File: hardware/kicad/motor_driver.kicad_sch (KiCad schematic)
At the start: 17 parts, among them J1 Conn_01x05_Pin, J2 TO_MOTOR, J3 5V_IN, J4 PRT-10811, U1 ULN2003A

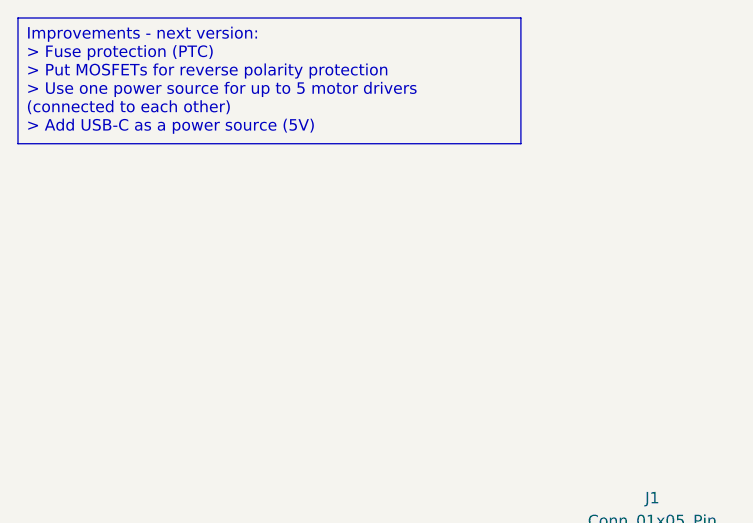
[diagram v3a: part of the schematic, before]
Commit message: feat: added pcb board and components placements
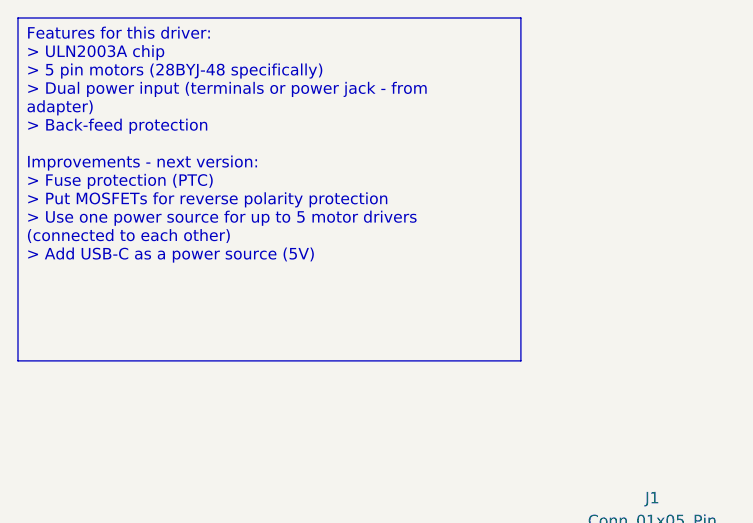
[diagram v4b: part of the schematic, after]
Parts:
- C1: footprint (none) -> Capacitor_THT:C_Rect_L4.6mm_W3.0mm_P2.50mm_MKS02_FKP02
- C2: footprint (none) -> Capacitor_THT:CP_Radial_D8.0mm_P3.50mm
- D1, D2: footprint (none) -> Diode_THT:D_DO-201AD_P15.24mm_Horizontal
- J4: footprint PRT-10811_SPK -> Power Jack:PRT-10811_SPK
- R1, R2, R3, R4, R5, R6, R7, R8: footprint (none) -> Resistor_THT:R_Axial_DIN0207_L6.3mm_D2.5mm_P10.16mm_Horizontal
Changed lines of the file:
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@@
 	(generator_version "9.0")
 	(paper "A4")
-	(text_box "Improvements - next version:\n> Fuse protection (PTC)\n> Put MOSFETs for reverse polarity protection\n> Use one power source for up to 5 motor drivers (connected to each other)\n> Add USB-C as a power source (5V)"
+	(text_box "Features for this driver:\n> ULN2003A chip\n> 5 pin motors (28BYJ-48 specifically)\n> Dual power input (terminals or power jack - from adapter)\n> Back-feed protection\n\nImprovements - next version:\n> Fuse protection (PTC)\n> Put MOSFETs for reverse polarity protection\n> Use one power source for up to 5 motor drivers (connected to each other)\n> Add USB-C as a power source (5V)"
 		(exclude_from_sim no)
 		(at 15.24 13.97 0)
-		(size 55.88 13.97)
+		(size 55.88 38.1)
 		(margins 0.9525 0.9525 0.9525 0.9525)
 		(stroke
@@
 			)
 		)
-		(property "Footprint" ""
+		(property "Footprint" "Capacitor_THT:C_Rect_L4.6mm_W3.0mm_P2.50mm_MKS02_FKP02"
 			(at 146.3548 88.9 0)
 			(effects
@@
 			)
 		)
-		(property "Footprint" ""
+		(property "Footprint" "Diode_THT:D_DO-201AD_P15.24mm_Horizontal"
 			(at 168.91 45.72 0)
 			(effects
@@
 			)
 		)
-		(property "Footprint" ""
+		(property "Footprint" "Capacitor_THT:CP_Radial_D8.0mm_P3.50mm"
 			(at 154.6352 88.9 0)
 			(effects
@@
 			)
 		)
-		(property "Footprint" ""
+		(property "Footprint" "Resistor_THT:R_Axial_DIN0207_L6.3mm_D2.5mm_P10.16mm_Horizontal"
 			(at 100.33 81.788 90)
 			(effects
@@
 			)
 		)
-		(property "Footprint" "PRT-10811_SPK"
+		(property "Footprint" "Power Jack:PRT-10811_SPK"
 			(at 180.34 45.72 0)
 			(effects
@@
 			)
 		)
-		(property "Footprint" ""
+		(property "Footprint" "Resistor_THT:R_Axial_DIN0207_L6.3mm_D2.5mm_P10.16mm_Horizontal"
 			(at 107.188 93.98 90)
 			(effects
@@
 			)
 		)
-		(property "Footprint" ""
+		(property "Footprint" "Resistor_THT:R_Axial_DIN0207_L6.3mm_D2.5mm_P10.16mm_Horizontal"
 			(at 100.33 74.168 90)
 			(effects
@@
 			)
 		)
-		(property "Footprint" ""
+		(property "Footprint" "Resistor_THT:R_Axial_DIN0207_L6.3mm_D2.5mm_P10.16mm_Horizontal"
 			(at 109.728 93.98 90)
 			(effects
@@
 			)
 		)
-		(property "Footprint" ""
+		(property "Footprint" "Resistor_THT:R_Axial_DIN0207_L6.3mm_D2.5mm_P10.16mm_Horizontal"
 			(at 112.268 93.98 90)
 			(effects
@@
 			)
 		)
-		(property "Footprint" ""
+		(property "Footprint" "Resistor_THT:R_Axial_DIN0207_L6.3mm_D2.5mm_P10.16mm_Horizontal"
 			(at 100.33 79.248 90)
 			(effects
@@
 			)
 		)
-		(property "Footprint" ""
+		(property "Footprint" "Diode_THT:D_DO-201AD_P15.24mm_Horizontal"
 			(at 170.18 62.23 0)
 			(effects
@@
 			)
 		)
-		(property "Footprint" ""
+		(property "Footprint" "Resistor_THT:R_Axial_DIN0207_L6.3mm_D2.5mm_P10.16mm_Horizontal"
 			(at 114.808 93.98 90)
 			(effects
@@
 			)
 		)
-		(property "Footprint" ""
+		(property "Footprint" "Resistor_THT:R_Axial_DIN0207_L6.3mm_D2.5mm_P10.16mm_Horizontal"
 			(at 100.33 76.708 90)
 			(effects

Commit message: perf: routed the components - PCB
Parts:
- removed J4: PRT-10811, Power Jack:PRT-10811_SPK, symbol Power Jack:PRT-10811
- added J4: DC-005-5A-2.0, DC-005-5A-2.0:XKB_DC-005-5A-2.0, symbol Power Jack:DC-005-5A-2.0
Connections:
- net +5V_COM: now reaches C1.1, C2.1, D1.1 (K), D2.1 (K), J2.1 (Pin_1), U1.9 (COM)
- net GND: now reaches C1.2, C2.2, J1.5 (Pin_5), J3.2 (Pin_2), R5.1, R6.1, R7.1, R8.1, U1.8 (GND)
- net GND: now also J4.2, J4.3
- net at D1.2 (A): now also J4.1
- net IN4: now reaches J1.4 (Pin_4), R4.1
- net IN1: now reaches J1.1 (Pin_1), R1.1
- net IN3: now reaches J1.3 (Pin_3), R3.1
- net IN2: now reaches J1.2 (Pin_2), R2.1
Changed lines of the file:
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@@
+		)
+	)
+	(label "IN3"
+		(at 93.98 77.47 0)
+		(effects
+			(font
+				(size 1.27 1.27)
+			)
+			(justify left bottom)
+		)
+	)
+	(label "+5V_COM"
+		(at 138.43 67.31 0)
+		(effects
+			(font
+				(size 1.27 1.27)
+			)
+			(justify left bottom)
+		)
+	)
+	(label "IN4"
+		(at 93.98 80.01 0)
+		(effects
+			(font
+				(size 1.27 1.27)
+			)
+			(justify left bottom)
+		)
+	)
+	(label "GND"
+		(at 93.98 82.55 0)
+		(effects
+			(font
+				(size 1.27 1.27)
+			)
+			(justify left bottom)
+		)
+	)
+	(label "IN2"
+		(at 93.98 74.93 0)
+		(effects
+			(font
+				(size 1.27 1.27)
+			)
+			(justify left bottom)
+		)
+	)
+	(label "IN1"
+		(at 93.98 72.39 0)
+		(effects
+			(font
+				(size 1.27 1.27)
+			)
+			(justify left bottom)
 		)
 	)
@@
 	)
 	(symbol
-		(lib_id "Power Jack:PRT-10811")
-		(at 180.34 45.72 180)
-		(unit 1)
-		(exclude_from_sim no)
-		(in_bom yes)
-		(on_board yes)
-		(dnp no)
-		(fields_autoplaced yes)
-		(property "Reference" "J4"
-			(at 212.09 41.9099 0)
-			(effects
-				(font
-					(size 1.524 1.524)
-				)
-				(justify right)
-			)
-		)
-		(property "Value" "PRT-10811"
-			(at 212.09 44.4499 0)
-			(effects
-				(font
-					(size 1.524 1.524)
-				)
-				(justify right)
-			)
-		)
-		(property "Footprint" "Power Jack:PRT-10811_SPK"
-			(at 180.34 45.72 0)
-			(effects
-				(font
-					(size 1.27 1.27)
-					(italic yes)
-				)
-				(hide yes)
-			)
-		)
-		(property "Datasheet" "PRT-10811"
-			(at 180.34 45.72 0)
-			(effects
-				(font
-					(size 1.27 1.27)
-					(italic yes)
-				)
-				(hide yes)
-			)
-		)
-		(property "Description" ""
-			(at 180.34 45.72 0)
-			(effects
-				(font
-					(size 1.27 1.27)
-				)
-				(hide yes)
-			)
-		)
-		(pin "3"
-		)
-		(pin "2"
-		)
-		(pin "1"
-		)
-		(instances
-			(project ""
-				(path "/b7a12314-1361-4fdf-a1f9-9f4ac4cac78f"
-					(reference "J4")
-					(unit 1)
-				)
-			)
-		)
-	)
-	(symbol
 		(lib_id "power:PWR_FLAG")
 		(at 179.07 40.64 0)
@@
 					(unit 1)
 				)
+			)
+		)
+	)
+	(symbol
+		(lib_id "Power Jack:DC-005-5A-2.0")
+		(at 187.96 43.18 180)
+		(unit 1)
+		(exclude_from_sim no)
+		(in_bom yes)
+		(on_board yes)
+		(dnp no)
+		(property "Reference" "J4"
+			(at 188.7311 52.07 0)
+			(effects
+				(font
+					(size 1.27 1.27)
+				)
+			)
+		)
+		(property "Value" "DC-005-5A-2.0"
+			(at 188.7311 49.53 0)
+			(effects
+				(font
+					(size 1.27 1.27)
+				)
+			)
+		)
+		(property "Footprint" "DC-005-5A-2.0:XKB_DC-005-5A-2.0"
+			(at 187.96 43.18 0)
+			(effects
+				(font
+					(size 1.27 1.27)
+				)
+				(justify bottom)
+				(hide yes)
+			)
+		)
+		(property "Datasheet" ""
+			(at 187.96 43.18 0)
+			(effects
+				(font
+					(size 1.27 1.27)
+				)
+				(hide yes)
+			)
+		)
+		(property "Description" ""
+			(at 187.96 43.18 0)
+			(effects
+				(font
+					(size 1.27 1.27)
+				)
+				(hide yes)
+			)
+		)
+		(property "MF" "XKB Industrial Precision"
+			(at 187.96 43.18 0)
+			(effects
+				(font
+					(size 1.27 1.27)
+				)
+				(justify bottom)
+				(hide yes)
+			)
+		)
+		(property "MAXIMUM_PACKAGE_HEIGHT" "11 mm"
+			(at 187.96 43.18 0)
+			(effects
+				(font
+					(size 1.27 1.27)
+				)
+				(justify bottom)
+				(hide yes)
+			)
+		)
+		(property "Package" "Package"
+			(at 187.96 43.18 0)
+			(effects
+				(font
+					(size 1.27 1.27)
+				)
+				(justify bottom)
+				(hide yes)
+			)
+		)
+		(property "Price" "None"
+			(at 187.96 43.18 0)
+			(effects
+				(font
+					(size 1.27 1.27)
+				)
+				(justify bottom)
+				(hide yes)
+			)
+		)
+		(property "Check_prices" "https://www.snapeda.com/parts/DC-005-5A-2.0/XKB+Connection/view-part/?ref=eda"
+			(at 187.96 43.18 0)
+			(effects
+				(font
+					(size 1.27 1.27)
+				)
+				(justify bottom)
+				(hide yes)
+			)
+		)
+		(property "STANDARD" "Manufacturer Recommendations"
+			(at 187.96 43.18 0)
+			(effects
+				(font
+					(size 1.27 1.27)
+				)
+				(justify bottom)
+				(hide yes)
+			)
+		)
+		(property "PARTREV" "A0"
+			(at 187.96 43.18 0)
+			(effects
+				(font
+					(size 1.27 1.27)
+				)
+				(justify bottom)
+				(hide yes)
+			)
+		)
+		(property "SnapEDA_Link" "https://www.snapeda.com/parts/DC-005-5A-2.0/XKB+Connection/view-part/?ref=snap"
+			(at 187.96 43.18 0)
+			(effects
+				(font
+					(size 1.27 1.27)
+				)
+				(justify bottom)
+				(hide yes)
+			)
+		)
+		(property "MP" "DC-005-5A-2.0"
+			(at 187.96 43.18 0)
+			(effects
+				(font
+					(size 1.27 1.27)
+				)
+				(justify bottom)
+				(hide yes)
+			)
+		)
+		(property "Description_1" "DC Power Receptacle Jack, Through Hole，Right Angle"
+			(at 187.96 43.18 0)
+			(effects
+				(font
+					(size 1.27 1.27)
+				)
+				(justify bottom)
+				(hide yes)
+			)
+		)
+		(property "Availability" "Not in stock"
+			(at 187.96 43.18 0)
+			(effects
+				(font
+					(size 1.27 1.27)
+				)
+				(justify bottom)
+				(hide yes)
+			)
+		)
+		(property "MANUFACTURER" "XKB"
+			(at 187.96 43.18 0)
+			(effects
+				(font
+					(size 1.27 1.27)
+				)
+				(justify bottom)
+				(hide yes)
+			)
+		)
+		(pin "1"
+		)
+		(pin "3"
+		)
+		(pin "2"
+		)
+		(instances
+			(project ""
+				(path "/b7a12314-1361-4fdf-a1f9-9f4ac4cac78f"
+					(reference "J4")
+					(unit 1)
+				)

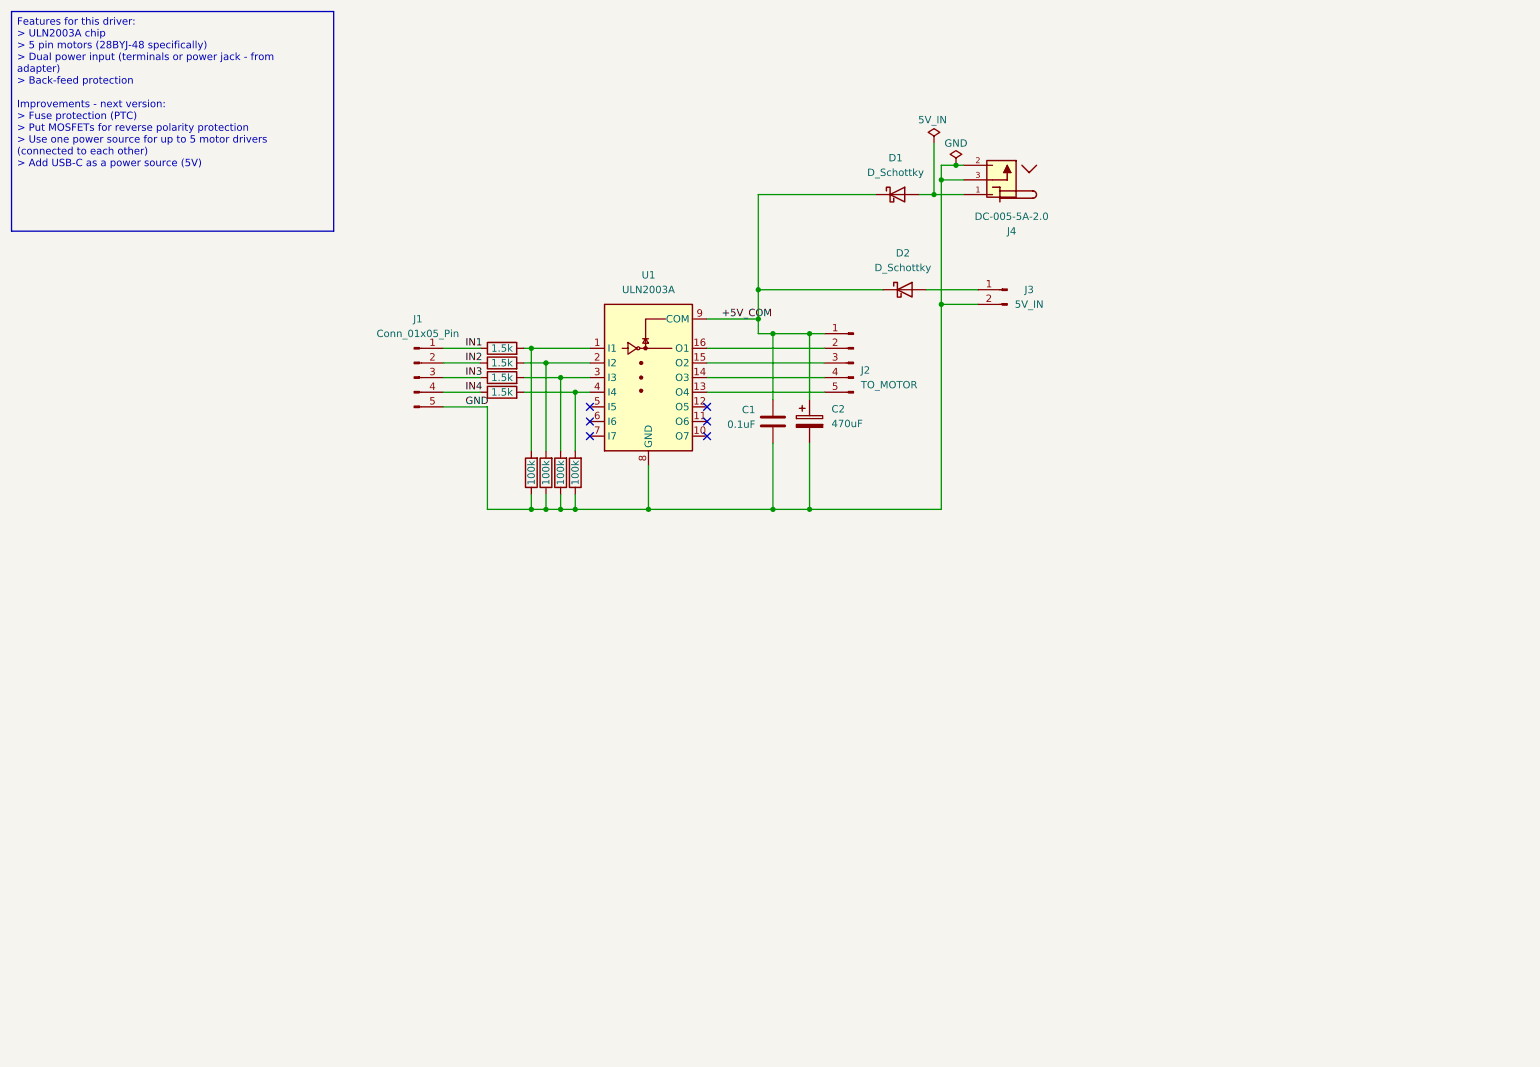
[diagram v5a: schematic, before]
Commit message: docs: added exports schematic & pcb
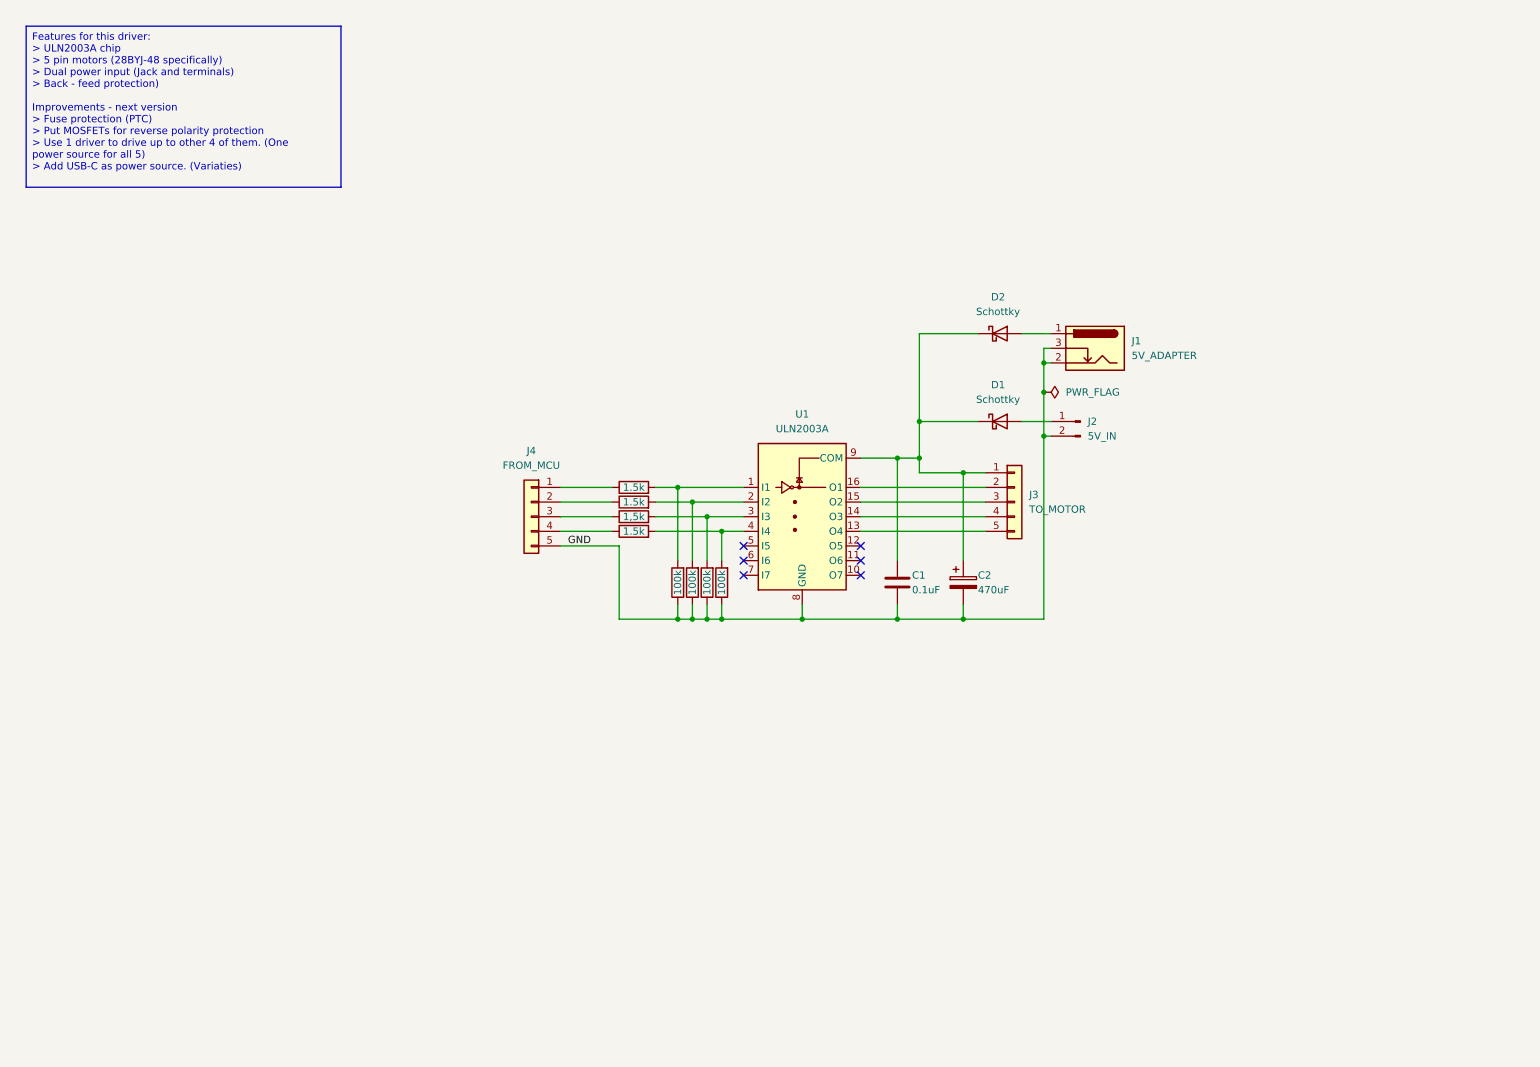
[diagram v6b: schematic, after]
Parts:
- removed J1: Conn_01x05_Pin, Connector_PinHeader_2.54mm:PinHeader_1x05_P2.54mm_Vertical, symbol Connector:Conn_01x05_Pin
- removed J2: TO_MOTOR, Connector_JST:JST_XH_B5B-XH-A_1x05_P2.50mm_Vertical, symbol Connector:Conn_01x05_Pin
- removed J3: 5V_IN, Connector_PinHeader_2.54mm:PinHeader_1x02_P2.54mm_Vertical, symbol Connector:Conn_01x02_Pin
- removed J4: DC-005-5A-2.0, DC-005-5A-2.0:XKB_DC-005-5A-2.0, symbol Power Jack:DC-005-5A-2.0
- added J1: 5V_ADAPTER, Connector_BarrelJack:BarrelJack_GCT_DCJ200-10-A_Horizontal, symbol Connector:Barrel_Jack_Switch
- added J2: 5V_IN, Connector_PinHeader_2.54mm:PinHeader_1x05_P2.54mm_Vertical, symbol Connector:Conn_01x02_Pin
- added J3: TO_MOTOR, Connector_JST:JST_XH_B5B-XH-A_1x05_P2.50mm_Vertical, symbol Connector_Generic:Conn_01x05
- added J4: FROM_MCU, Connector_PinHeader_2.54mm:PinHeader_1x05_P2.54mm_Vertical, symbol Connector_Generic:Conn_01x05
- C1: footprint Capacitor_THT:C_Rect_L4.6mm_W3.0mm_P2.50mm_MKS02_FKP02 -> Capacitor_THT:C_Rect_L7.2mm_W3.5mm_P5.00mm_FKS2_FKP2_MKS2_MKP2
- C2: footprint Capacitor_THT:CP_Radial_D8.0mm_P3.50mm -> Capacitor_THT:CP_Radial_D10.0mm_P5.00mm
- D1, D2: value D_Schottky -> Schottky
- R3: value 1.5k -> 1,5k
- U1: footprint Package_DIP:DIP-16_W7.62mm -> Package_DIP:DIP-16_W7.62mm_Socket
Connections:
- net GND: now also J1.2, J1.3, J2.2 (Pin_2), J4.5 (Pin_5)
- net at D1.2 (A): now also J2.1 (Pin_1)
- net at U1.16 (O1): now also J3.2 (Pin_2)
- net at U1.15 (O2): now also J3.3 (Pin_3)
- net at U1.14 (O3): now also J3.4 (Pin_4)
- net at U1.13 (O4): now also J3.5 (Pin_5)
- net at D2.2 (A): now also J1.1
- net +5V_COM: no longer names the net of C1.1, C2.1, D1.1 (K), D2.1 (K), U1.9 (COM)
- net +5V_COM: now also J3.1 (Pin_1)
- net IN1: no longer names the net of R1.1
- net IN1: now also J4.1 (Pin_1)
- net IN2: no longer names the net of R2.1
- net IN2: now also J4.2 (Pin_2)
- net IN3: no longer names the net of R3.1
- net IN3: now also J4.3 (Pin_3)
- net IN4: no longer names the net of R4.1
- net IN4: now also J4.4 (Pin_4)

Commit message: docs: bom generated and updated schematics
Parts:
- J2: footprint Connector_PinHeader_2.54mm:PinHeader_1x05_P2.54mm_Vertical -> Connector_PinHeader_2.54mm:PinHeader_1x02_P2.54mm_Vertical
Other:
- note added: "02-03-2026"
- note added: "1.0"
- note added: "motor_driver"
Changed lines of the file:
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@@
     (effects (font (size 1.27 1.27)) (justify left top))
+  )
+  (text "motor_driver" (at 193.04 190.5 0)
+    (effects (font (size 2 2) (thickness 0.4) bold) (justify left bottom))
+  )
+  (text "02-03-2026" (at 215.9 194.31 0)
+    (effects (font (size 2 2) bold) (justify left bottom))
+  )
+  (text "1.0" (at 271.78 194.31 0)
+    (effects (font (size 2 2) (thickness 0.4) bold) (justify left bottom))
   )
   (label "GND" (at 111.76 106.68 0) (fields_autoplaced)
@@
       (effects (font (size 1.27 1.27)) (justify right))
     )
-    (property "Footprint" "Connector_PinHeader_2.54mm:PinHeader_1x05_P2.54mm_Vertical" (at 200.66 85.09 0)
+    (property "Footprint" "Connector_PinHeader_2.54mm:PinHeader_1x02_P2.54mm_Vertical" (at 200.66 85.09 0)
       (effects (font (size 1.27 1.27)) hide)
     )
@@
         )
       )
+    )
+  )
+  (symbol (lib_id "Logo:LOGO") (at 66.04 26.67 0) (unit 1)
+    (in_bom yes) (on_board yes) (dnp no) (fields_autoplaced)
+    (property "Reference" "#G1" (at 66.04 24.5047 0)
+      (effects (font (size 1.27 1.27)) hide)
+    )
+    (property "Value" "LOGO" (at 66.04 28.8353 0)
+      (effects (font (size 1.27 1.27)) hide)
+    )
+    (property "Footprint" "" (at 66.04 26.67 0)
+      (effects (font (size 1.27 1.27)) hide)
+    )
+    (property "Datasheet" "" (at 66.04 26.67 0)
+      (effects (font (size 1.27 1.27)) hide)
+    )
+    (instances
+      (project "motor_driver"
+        (path "/389f229a-cd60-4068-8ff2-e2ecc24ad1c0"
+          (reference "#G1") (unit 1)
+        )
+      )
